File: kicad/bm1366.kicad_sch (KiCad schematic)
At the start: 57 parts, among them J3 Conn_01x05, Q5 BSS138, U10 +0V8, U11 +0V8, U12 +0V8, U14 BM1366_mode1, U15 2N7001TDCK, U16 2N7001TDCK, U2 +0V8, U4 +0V8, U5 MCP1824T-1802E, U6 MCP1824T-0802E, U7 25MHz, U8 +0V8, U9 +0V8

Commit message: fixed heatsink order number, updated BOM
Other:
- title: BM1366 bitaxe -> BM1366 PiAxe
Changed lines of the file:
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@@
   (paper "A")
   (title_block
-    (title "BM1366 bitaxe")
+    (title "BM1366 PiAxe")
     (date "2023-10-10")
     (rev "202")

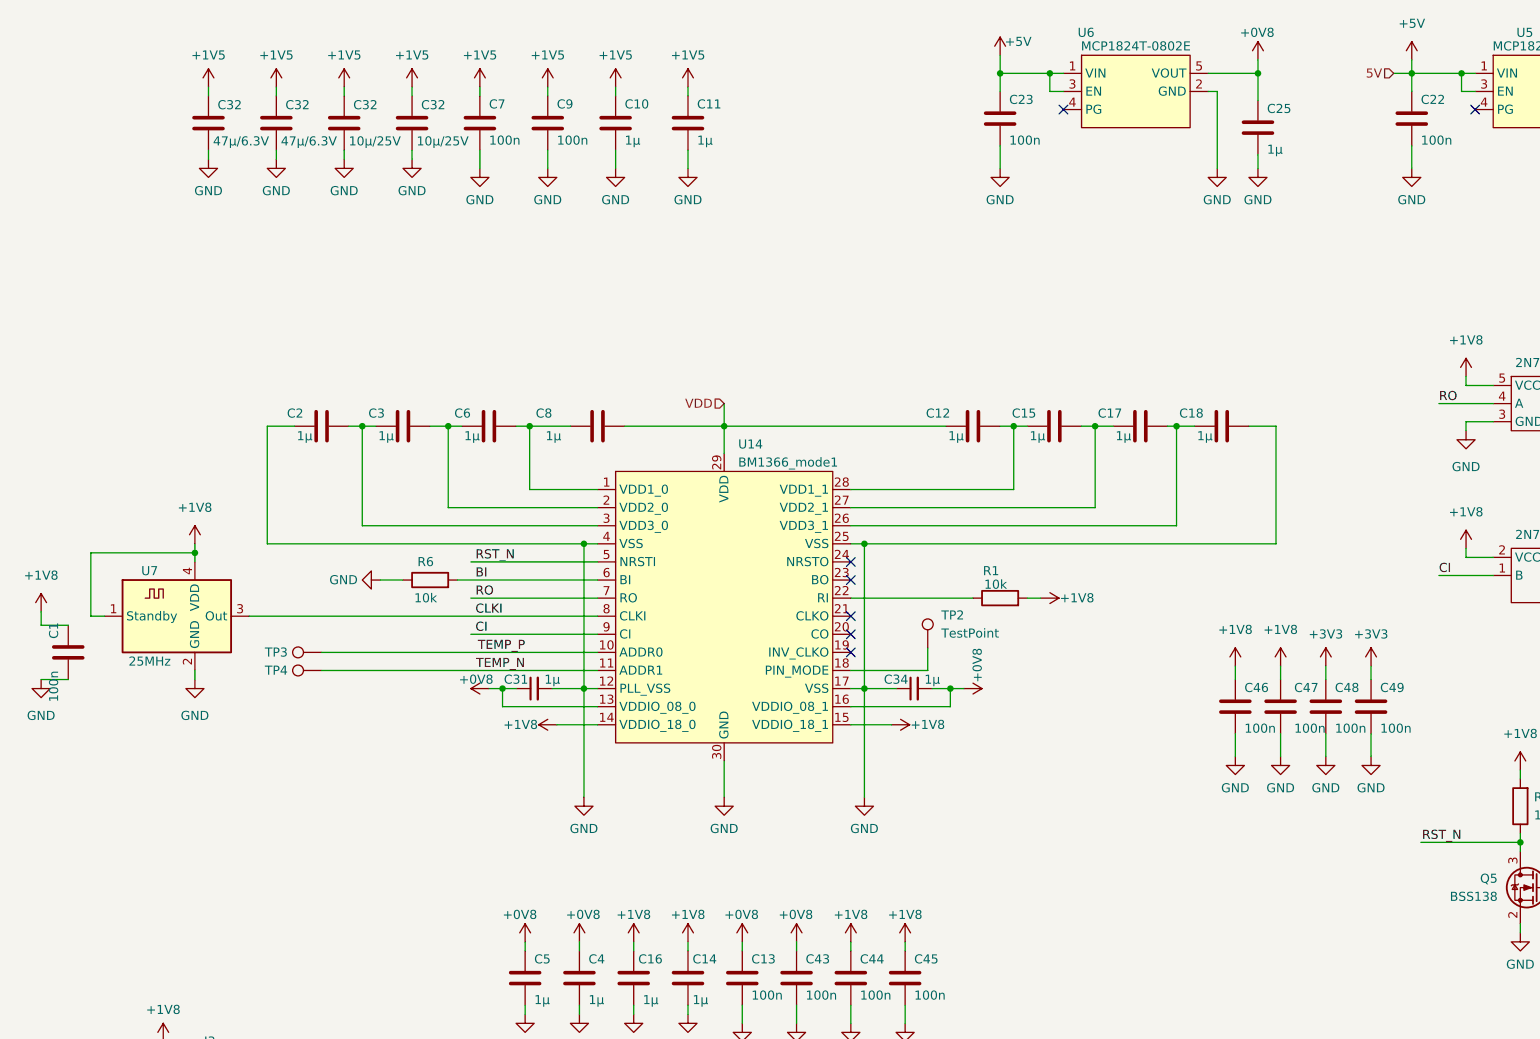
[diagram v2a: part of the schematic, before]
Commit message: fixed net labeling to 1.2V
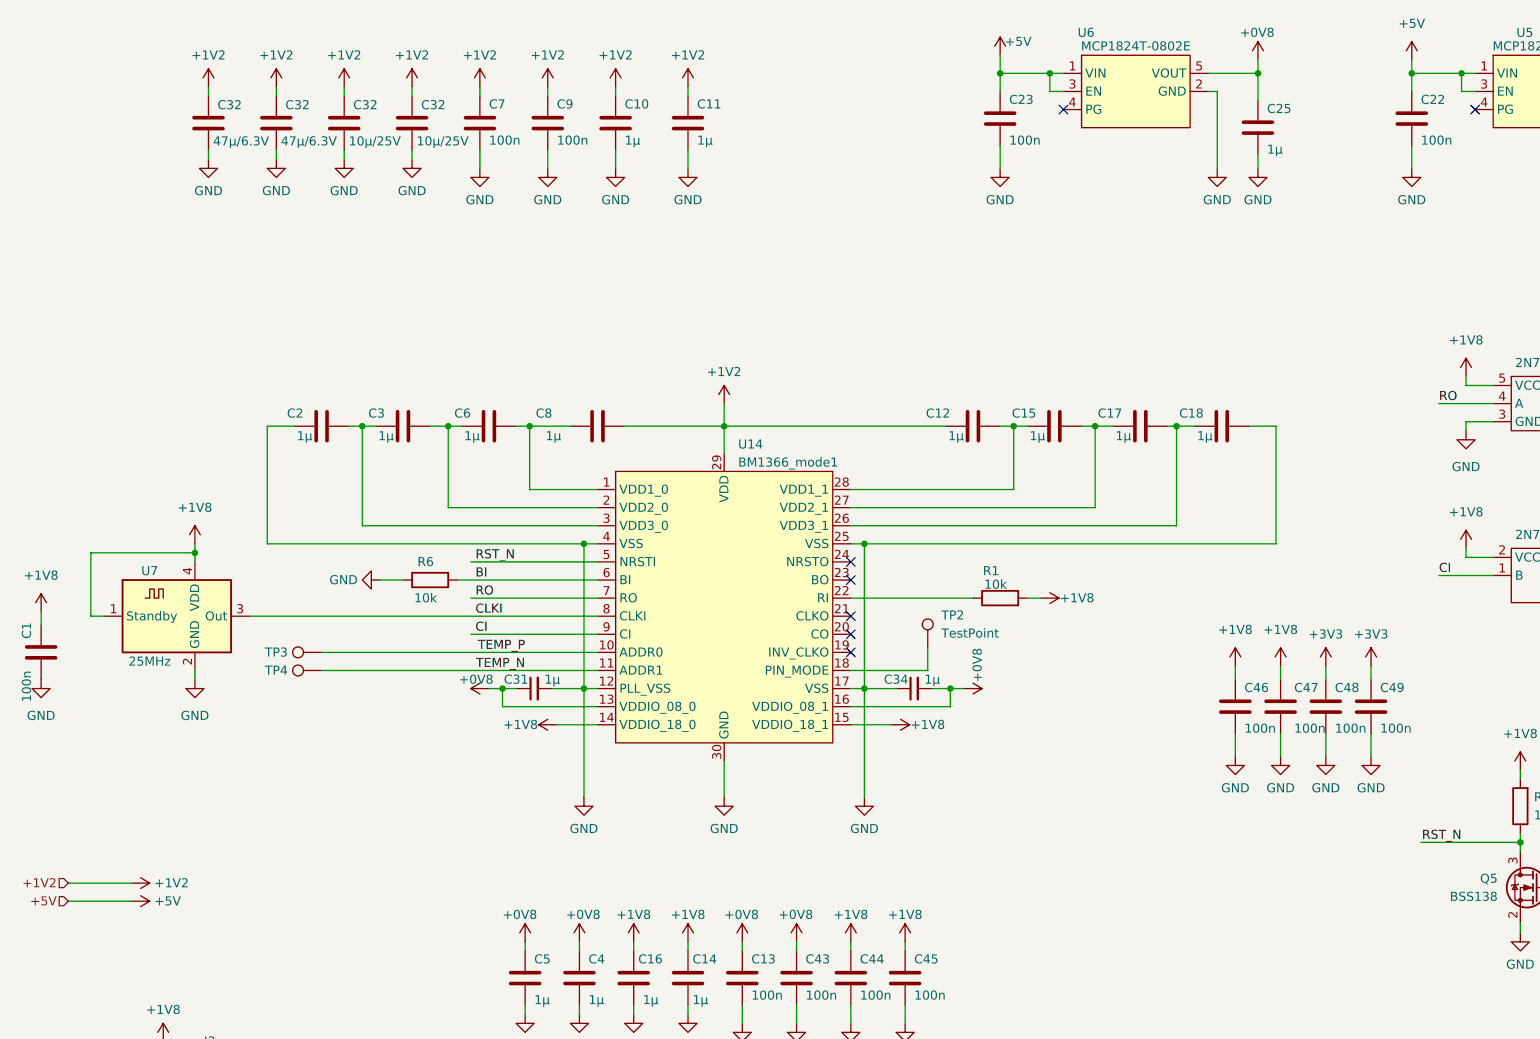
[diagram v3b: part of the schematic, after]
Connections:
- net VDD is gone; now on net +1V2: C12.1, C8.2, U14.29 (VDD)
- net +1V5 renamed +1V2
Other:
- moved on the sheet: C1

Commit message: initial commit before replacing power supply
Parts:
- removed C10, C11, C24, C25, C4, C5: 1µ, Capacitor_SMD:C_0805_2012Metric, symbol Device:C
- removed C13, C22, C23, C7, C9: 100n, Capacitor_SMD:C_0805_2012Metric, symbol Device:C
- removed C31, C34: 1µ, Capacitor_SMD:C_0805_2012Metric, symbol Device:C_Small
- removed C32 (x2): 47µ/6.3V, Capacitor_SMD:C_1210_3225Metric, symbol Device:C
- removed C32 (x2): 10µ/25V, Capacitor_SMD:C_1210_3225Metric, symbol Device:C
- removed J3: Conn_01x05, Connector_PinHeader_2.54mm:PinHeader_1x05_P2.54mm_Vertical, symbol Connector_Generic:Conn_01x05
- removed R1: 10k, Resistor_SMD:R_0805_2012Metric, symbol Device:R
- removed U4: +0V8, symbol mylib7:+0V8
- removed U5: MCP1824T-1802E, Package_TO_SOT_SMD:SOT-23-5, symbol bitaxe:MCP1824
- removed U6: MCP1824T-0802E, Package_TO_SOT_SMD:SOT-23-5, symbol bitaxe:MCP1824
- added C26, C27, C29, C31: 10µ, Capacitor_SMD:C_0805_2012Metric, symbol Device:C
- added C28, C30, C32, C33, C34, C36, C37, C38, C40, C41, C44, C46, C47, C51, C57, C61, C63, C64, C65, C67, C68, C70, C72, C73, C74, C75, C76, C77, C78, C79, C80: 1µ, Capacitor_SMD:C_0805_2012Metric, symbol Device:C
- added C39, C45, C48: 330µ/6.3V, Capacitor_Tantalum_SMD:CP_EIA-7343-15_Kemet-W, symbol Device:C_Polarized
- added C49, C53, C55, C59: 100n, Capacitor_SMD:C_0805_2012Metric, symbol Device:C
- added R20, R21, R22, R23: 10k, Resistor_SMD:R_0805_2012Metric, symbol Device:R
- added TP10, TP11, TP12, TP13, TP4, TP5, TP7, TP8, TP9: TestPoint, TestPoint:TestPoint_Pad_D1.5mm, symbol Connector:TestPoint
- added U13, U14, U15, U16, U18, U22, U23, U24, U27, U28: +0V8, symbol mylib7:+0V8
- added U20, U25, U26: BM1366_mode1, bitaxe:BM1366, symbol bitaxe:BM1366_mode1
- added U31: MCP1825S, symbol Regulator_Linear:MCP1825S
- C43: value 100n -> 1µ; PARTNO 0402X104K100CT -> EMK105BJ105MV-F
- C58: renamed from C44; value 100n -> 1µ
- C60: renamed from C45; value 100n -> 1µ
- renumbered C1 to C25, C2 to C35, C3 to C42, C6 to C50, C16 to C52, C14 to C54, C8 to C56, C12 to C62, C15 to C66, C17 to C69, C18 to C71, C46 to C81, C47 to C82, C48 to C83, C49 to C84, Q5 to Q7, R6 to R19, R8 to R24, R9 to R25, TP3 to TP2, TP4 to TP3, TP2 to TP6, U2 to U17, U14 to U19, U8 to U21, U15 to U29, U16 to U30, U7 to U8
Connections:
- net +0V8: now also C28.2, C30.2, C32.2, C34.2, C37.2, C40.2, C44.2, C47.2, U13.1 (+0V8), U14.1 (+0V8), U15.1 (+0V8), U16.1 (+0V8), U18.1 (+0V8), U20.13 (VDDIO_08_0), U20.16 (VDDIO_08_1), U22.1 (+0V8), U23.1 (+0V8), U24.1 (+0V8), U25.13 (VDDIO_08_0), U25.16 (VDDIO_08_1), U26.13 (VDDIO_08_0), U26.16 (VDDIO_08_1), U27.1 (+0V8), U28.1 (+0V8); no longer C43.1
- net +1V2: now also C26.1, C27.1, C29.1, C31.1, C33.1, C38.1, C39.1, C41.1, C45.1, C46.1, C48.1, C49.1, C53.1, C55.1, C57.2, C59.1, C63.1, C73.1, C74.1, U20.29 (VDD), U25.29 (VDD), U26.29 (VDD)
- net +1V8: now also C61.1, C64.1, C65.1, C68.1, R20.2, R21.2, R22.2, R23.2, U20.14 (VDDIO_18_0), U20.15 (VDDIO_18_1), U25.14 (VDDIO_18_0), U25.15 (VDDIO_18_1), U26.14 (VDDIO_18_0), U26.15 (VDDIO_18_1)
- net GND: now also C26.2, C27.2, C28.1, C29.2, C30.1, C31.2, C32.1, C33.2, C34.1, C36.1, C37.1, C38.2, C39.2, C40.1, C41.2, C44.1, C45.2, C46.2, C47.1, C48.2, C49.2, C53.2, C55.2, C59.2, C61.2, C64.2, C65.2, C68.2, C72.2, C79.2, C80.2, U20.12 (PLL_VSS), U20.17 (VSS), U20.25 (VSS), U20.30 (GND), U20.4 (VSS), U25.12 (PLL_VSS), U25.17 (VSS), U25.25 (VSS), U25.30 (GND), U25.4 (VSS), U26.12 (PLL_VSS), U26.17 (VSS), U26.25 (VSS), U26.30 (GND), U26.4 (VSS); no longer C43.2
- net at C69.2, C71.1, U19.26 (VDD3_1): now also U25.3 (VDD3_0)
- net at C66.2, C69.1, U19.27 (VDD2_1): now also U25.2 (VDD2_0)
- net at C62.2, C66.1, U19.28 (VDD1_1): now also U25.1 (VDD1_0)
- net at U19.20 (CO): now also U25.9 (CI)
- net at U19.21 (CLKO): now also U25.8 (CLKI)
- net at U19.22 (RI): now also R20.1, U25.7 (RO)
- net at U19.23 (BO): now also U25.6 (BI)
- net at U19.24 (NRSTO): now also U25.5 (NRSTI)
- net TEMP_N: no longer names the net of TP3.1, U19.11 (ADDR1)
- net TEMP_P: no longer names the net of TP2.1, U19.10 (ADDR0)
- new net: C67.2, C70.1, U20.27 (VDD2_1), U26.2 (VDD2_0)
- new net: C70.2, C72.1, U20.26 (VDD3_1), U26.3 (VDD3_0)
- new net: C36.2, C43.1, U20.3 (VDD3_0)
- new net: C43.2, C51.1, U20.2 (VDD2_0)
- new net: C74.2, C76.1, U26.28 (VDD1_1)
- new net: C76.2, C78.1, U26.27 (VDD2_1)
- new net: R21.1, U20.22 (RI), U26.7 (RO)
- new net: TP13.1, U25.18 (PIN_MODE)
- new net: C63.2, C67.1, U20.28 (VDD1_1), U26.1 (VDD1_0)
- new net: C73.2, C75.1, U25.28 (VDD1_1)
- new net: TP7.1, U20.18 (PIN_MODE)
- new net: TP8.1, U25.10 (ADDR0)
- new net: TP9.1, U25.11 (ADDR1)
- new net: U20.9 (CI), U25.20 (CO)
- new net: U20.8 (CLKI), U25.21 (CLKO)
- new net: R23.1, U20.7 (RO), U25.22 (RI)
- new net: U20.6 (BI), U25.23 (BO)
- new net: U20.5 (NRSTI), U25.24 (NRSTO)
- new net: C77.2, C79.1, U25.26 (VDD3_1)
- new net: C75.2, C77.1, U25.27 (VDD2_1)
- new net: C78.2, C80.1, U26.26 (VDD3_1)
- new net: C51.2, C57.1, U20.1 (VDD1_0)
- new net: TP10.1, U26.10 (ADDR0)
- new net: R22.1, U26.22 (RI)
- new net: TP11.1, U26.11 (ADDR1)
- new net: TP12.1, U26.18 (PIN_MODE)
- new net: U20.24 (NRSTO), U26.5 (NRSTI)
- new net: U20.23 (BO), U26.6 (BI)
- new net: U20.21 (CLKO), U26.8 (CLKI)
- new net: U20.20 (CO), U26.9 (CI)
- new net: TP4.1, U20.10 (ADDR0)
- new net: TP5.1, U20.11 (ADDR1)
- no-connect marks 7 -> 8
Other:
- note removed: "1V8 Serial Debug Headers"
- moved on the sheet: C25, C35, C42, C50, C52, C54, C56, C58, C60, C62, C66, C69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

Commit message: updated gerber, bom
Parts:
- removed U31: MCP1825S, symbol Regulator_Linear:MCP1825S
- added C93, C94: 1µ, Capacitor_SMD:C_0805_2012Metric, symbol Device:C
- added J2: Conn_01x06, Connector_PinHeader_1.27mm:PinHeader_1x06_P1.27mm_Vertical, symbol Connector_Generic:Conn_01x06
- added U31, U34: +0V8, symbol mylib7:+0V8
- C25, C58, C60, C65, C68, C81, C82, C83, C84: PARTNO 0402X104K100CT -> (none)
- C26, C27, C29, C31: value 10µ -> 10µ/16V; PARTNO EMK105BJ105MV-F -> (none)
- C28, C30, C32, C33, C34, C35, C36, C37, C38, C40, C41, C42, C43, C44, C46, C47, C49, C50, C51, C52, C53, C54, C55, C56, C57, C59, C61, C62, C63, C64, C66, C67, C69, C70, C71, C72, C73, C74, C75, C76, C77, C78, C79, C80: PARTNO EMK105BJ105MV-F -> (none)
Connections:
- net +0V8: now also J2.2 (Pin_2), U31.1 (+0V8), U34.1 (+0V8)
- net +1V2: now also C93.2, C94.2
- net +1V8: now also J2.1 (Pin_1)
- net CI: now also J2.5 (Pin_5)
- net GND: now also J2.6 (Pin_6)
- net RO: now also J2.4 (Pin_4)
- net RST_N: now also J2.3 (Pin_3)
- net at C63.2, C67.1, U20.28 (VDD1_1)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: now also C94.1
- net at C62.2, C66.1, U19.28 (VDD1_1)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: now also C93.1
- net RST renamed RESET
- net RX renamed RXD
- net TX renamed TXD
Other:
- moved on the sheet: C25, C26, C27, C28, C29, C30, C31, C32, C33, C34, C35, C36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

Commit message: v0.02
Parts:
- removed U29, U30: 2N7001TDCK, Package_TO_SOT_SMD:SOT-353_SC-70-5, symbol mylib7:2N7001TDCKR
- added U29, U38: TXU0101, Package_TO_SOT_SMD:SOT-363_SC-70-6, symbol mylib7:TXU0101DCK
- J2, U31, U34: Distributor (none) -> -
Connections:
- net +1V8: now also U29.5 (OE), U29.6 (VCCB), U38.1 (VCCA)
- net +3V3: now also U29.1 (VCCA), U38.5 (OE), U38.6 (VCCB)
- net CI: now also U29.4 (BY)
- net GND: now also U29.2 (GND), U38.2 (GND)
- net RO: now also U38.3 (A)
- net RXD: now also U38.4 (BY)
- net TXD: now also U29.3 (A)
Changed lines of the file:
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@@
   (junction (at 197.485 50.8) (diameter 0) (color 0 0 0 0)
   )
+  (junction (at 363.22 45.085) (diameter 0) (color 0 0 0 0)
+  )
   (junction (at 155.575 135.89) (diameter 0) (color 0 0 0 0)
   )
@@
   (junction (at 197.485 143.51) (diameter 0) (color 0 0 0 0)
   )
+  (junction (at 337.82 69.215) (diameter 0) (color 0 0 0 0)
+  )
   (no_connect (at 234.95 73.66))
   (no_connect (at 153.67 158.75))
@@
     (stroke (width 0) (type default))
   )
+  (wire (pts (xy 341.63 74.295) (xy 337.82 74.295))
+    (stroke (width 0) (type default))
+  )
   (wire (pts (xy 64.77 207.01) (xy 64.77 208.28))
     (stroke (width 0) (type default))
@@
     (stroke (width 0) (type default))
   )
+  (wire (pts (xy 337.82 74.295) (xy 337.82 69.215))
+    (stroke (width 0) (type default))
+  )
   (wire (pts (xy 194.945 76.2) (xy 199.39 76.2))
     (stroke (width 0) (type default))
@@
     (stroke (width 0) (type default))
   )
+  (wire (pts (xy 363.22 50.165) (xy 363.22 45.085))
+    (stroke (width 0) (type default))
+  )
   (wire (pts (xy 236.855 50.8) (xy 236.855 41.91))
     (stroke (width 0) (type default))
@@
     (stroke (width 0) (type default))
   )
+  (wire (pts (xy 359.41 50.165) (xy 363.22 50.165))
+    (stroke (width 0) (type default))
+  )
   (wire (pts (xy 114.3 207.01) (xy 114.3 208.28))
     (stroke (width 0) (type default))
@@
     )
   )
+  (symbol (lib_id "mylib7:TXU0101DCK") (at 350.52 47.625 0) (unit 1)
+    (in_bom yes) (on_board yes) (dnp no) (fields_autoplaced)
+    (property "Reference" "U38" (at 350.52 39.37 0)
+      (effects (font (size 1.27 1.27)))
+    )
+    (property "Value" "TXU0101" (at 350.52 41.91 0)
+      (effects (font (size 1.27 1.27)))
+    )
+    (property "Footprint" "Package_TO_SOT_SMD:SOT-363_SC-70-6" (at 349.25 45.085 0)
+      (effects (font (size 1.27 1.27)) hide)
+    )
+    (property "Datasheet" "" (at 349.25 45.085 0)
+      (effects (font (size 1.27 1.27)) hide)
+    )
+    (property "Distributor" "D" (at 350.52 47.625 0)
+      (effects (font (size 1.27 1.27)) hide)
+    )
+    (property "Manufacturer" "TXU0101DCKR" (at 350.52 47.625 0)
+      (effects (font (size 1.27 1.27)) hide)
+    )
+    (property "OrderNr" "296-TXU0101DCKRCT-ND" (at 350.52 47.625 0)
+      (effects (font (size 1.27 1.27)) hide)
+    )
+    (pin "1")
+    (pin "2")
+    (pin "3")
+    (pin "4")
+    (pin "5")
+    (pin "6")
+    (instances
+      (project "piaxe"
+        (path "/e63e39d7-6ac0-4ffd-8aa3-1841a4541b55/4cf9c075-d009-4c35-9949-adda70ae20c7"
+          (reference "U38") (unit 1)
+        )
+      )
+    )
+  )
   (symbol (lib_id "power:+1V2") (at 37.465 34.925 270) (unit 1)
     (in_bom yes) (on_board yes) (dnp no) (fields_autoplaced)
@@
     )
   )
-  (symbol (lib_id "mylib7:2N7001TDCKR") (at 350.52 47.625 0) (unit 1)
-    (in_bom yes) (on_board yes) (dnp no) (fields_autoplaced)
-    (property "Reference" "U29" (at 350.52 39.37 0)
-      (effects (font (size 1.27 1.27)))
-    )
-    (property "Value" "2N7001TDCK" (at 350.52 41.91 0)
-      (effects (font (size 1.27 1.27)))
-    )
-    (property "Footprint" "Package_TO_SOT_SMD:SOT-353_SC-70-5" (at 347.98 47.625 0)
-      (effects (font (size 1.27 1.27)) hide)
-    )
-    (property "Datasheet" "" (at 347.98 47.625 0)
-      (effects (font (size 1.27 1.27)) hide)
-    )
-    (property "Distributor" "D" (at 350.52 47.625 0)
-      (effects (font (size 1.27 1.27)) hide)
-    )
-    (property "Manufacturer" "2N7001TDCKR" (at 350.52 47.625 0)
-      (effects (font (size 1.27 1.27)) hide)
-    )
-    (property "OrderNr" "296-50213-1-ND" (at 350.52 47.625 0)
-      (effects (font (size 1.27 1.27)) hide)
-    )
-    (pin "1")
-    (pin "2")
-    (pin "3")
-    (pin "4")
-    (pin "5")
-    (instances
-      (project "piaxe"
-        (path "/e63e39d7-6ac0-4ffd-8aa3-1841a4541b55/4cf9c075-d009-4c35-9949-adda70ae20c7"
-          (reference "U29") (unit 1)
-        )
-      )
-    )
-  )
   (symbol (lib_id "power:+1V8") (at 159.385 83.82 270) (unit 1)
     (in_bom yes) (on_board yes) (dnp no)
@@
     )
   )
+  (symbol (lib_id "power:+1V2") (at 120.015 27.305 0) (unit 1)
+    (in_bom yes) (on_board yes) (dnp no) (fields_autoplaced)
+    (property "Reference" "#PWR01" (at 120.015 31.115 0)
+      (effects (font (size 1.27 1.27)) hide)
+    )
+    (property "Value" "+1V2" (at 120.015 22.86 0)
+      (effects (font (size 1.27 1.27)))
+    )
+    (property "Footprint" "" (at 120.015 27.305 0)
+      (effects (font (size 1.27 1.27)) hide)
+    )
+    (property "Datasheet" "" (at 120.015 27.305 0)
+      (effects (font (size 1.27 1.27)) hide)
+    )
+    (pin "1")
+    (instances
+      (project "piaxe"
+        (path "/e63e39d7-6ac0-4ffd-8aa3-1841a4541b55/4cf9c075-d009-4c35-9949-adda70ae20c7"
+          (reference "#PWR01") (unit 1)
+        )
+      )
+    )
+  )
   (symbol (lib_id "power:+1V2") (at 52.705 236.855 0) (unit 1)
     (in_bom yes) (on_board yes) (dnp no) (fields_autoplaced)
@@
     )
   )
-  (symbol (lib_id "mylib7:2N7001TDCKR") (at 350.52 71.755 0) (mirror y) (unit 1)
-    (in_bom yes) (on_board yes) (dnp no)
-    (property "Reference" "U30" (at 350.52 63.5 0)
-      (effects (font (size 1.27 1.27)))
-    )
-    (property "Value" "2N7001TDCK" (at 350.52 66.04 0)
-      (effects (font (size 1.27 1.27)))
-    )
-    (property "Footprint" "Package_TO_SOT_SMD:SOT-353_SC-70-5" (at 353.06 71.755 0)
-      (effects (font (size 1.27 1.27)) hide)
-    )
-    (property "Datasheet" "" (at 353.06 71.755 0)
-      (effects (font (size 1.27 1.27)) hide)
-    )
-    (property "Distributor" "D" (at 350.52 71.755 0)
-      (effects (font (size 1.27 1.27)) hide)
-    )
-    (property "Manufacturer" "2N7001TDCKR" (at 350.52 71.755 0)
-      (effects (font (size 1.27 1.27)) hide)
-    )
-    (property "OrderNr" "296-50213-1-ND" (at 350.52 71.755 0)
-      (effects (font (size 1.27 1.27)) hide)
-    )
-    (pin "1")
-    (pin "2")
-    (pin "3")
-    (pin "4")
-    (pin "5")
-    (instances
-      (project "piaxe"
-        (path "/e63e39d7-6ac0-4ffd-8aa3-1841a4541b55/4cf9c075-d009-4c35-9949-adda70ae20c7"
-          (reference "U30") (unit 1)
-        )
-      )
-    )
-  )
   (symbol (lib_id "mylib7:+0V8") (at 64.77 198.12 0) (unit 1)
     (in_bom yes) (on_board yes) (dnp no)
@@
     )
   )
+  (symbol (lib_id "power:PWR_FLAG") (at 120.015 27.305 180) (unit 1)
+    (in_bom yes) (on_board yes) (dnp no) (fields_autoplaced)
+    (property "Reference" "#FLG02" (at 120.015 29.21 0)
+      (effects (font (size 1.27 1.27)) hide)
+    )
+    (property "Value" "PWR_FLAG" (at 120.015 31.75 0)
+      (effects (font (size 1.27 1.27)))
+    )
+    (property "Footprint" "" (at 120.015 27.305 0)
+      (effects (font (size 1.27 1.27)) hide)
+    )
+    (property "Datasheet" "~" (at 120.015 27.305 0)
+      (effects (font (size 1.27 1.27)) hide)
+    )
+    (pin "1")
+    (instances
+      (project "piaxe"
+        (path "/e63e39d7-6ac0-4ffd-8aa3-1841a4541b55/4cf9c075-d009-4c35-9949-adda70ae20c7"
+          (reference "#FLG02") (unit 1)
+        )
+      )
+    )
+  )
   (symbol (lib_id "Device:C_Polarized") (at 186.69 203.2 0) (unit 1)
     (in_bom yes) (on_board yes) (dnp no)
@@
       (effects (font (size 1.27 1.27)) hide)
     )
+    (property "Distributor" "-" (at 260.985 238.76 0)
+      (effects (font (size 1.27 1.27)) hide)
+    )
     (pin "1")
     (instances
@@
     )
   )
+  (symbol (lib_id "mylib7:TXU0101DCK") (at 350.52 71.755 0) (mirror y) (unit 1)
+    (in_bom yes) (on_board yes) (dnp no)
+    (property "Reference" "U29" (at 350.52 63.5 0)
+      (effects (font (size 1.27 1.27)))
+    )
+    (property "Value" "TXU0101" (at 350.52 66.04 0)
+      (effects (font (size 1.27 1.27)))
+    )
+    (property "Footprint" "Package_TO_SOT_SMD:SOT-363_SC-70-6" (at 351.79 69.215 0)
+      (effects (font (size 1.27 1.27)) hide)
+    )
+    (property "Datasheet" "" (at 351.79 69.215 0)
+      (effects (font (size 1.27 1.27)) hide)
+    )
+    (property "Distributor" "D" (at 350.52 71.755 0)
+      (effects (font (size 1.27 1.27)) hide)
+    )
+    (property "Manufacturer" "TXU0101DCKR" (at 350.52 71.755 0)
+      (effects (font (size 1.27 1.27)) hide)
+    )
+    (property "OrderNr" "296-TXU0101DCKRCT-ND" (at 350.52 71.755 0)
+      (effects (font (size 1.27 1.27)) hide)
+    )
+    (pin "1")
+    (pin "2")
+    (pin "3")
+    (pin "4")
+    (pin "5")
+    (pin "6")
+    (instances
+      (project "piaxe"
+        (path "/e63e39d7-6ac0-4ffd-8aa3-1841a4541b55/4cf9c075-d009-4c35-9949-adda70ae20c7"
+          (reference "U29") (unit 1)
+        )
+      )
+    )
+  )
   (symbol (lib_id "power:GND") (at 324.485 55.88 0) (mirror y) (unit 1)
     (in_bom yes) (on_board yes) (dnp no) (fields_autoplaced)
@@
       (effects (font (size 1.27 1.27)) hide)
     )
+    (property "Distributor" "-" (at 37.465 38.735 0)
+      (effects (font (size 1.27 1.27)) hide)
+    )
     (pin "1")
     (instances
@@
       (effects (font (size 1.27 1.27)) hide)
     )
+    (property "Distributor" "-" (at 268.605 241.3 0)
+      (effects (font (size 1.27 1.27)) hide)
+    )
